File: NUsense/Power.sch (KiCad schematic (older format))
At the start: 13 parts

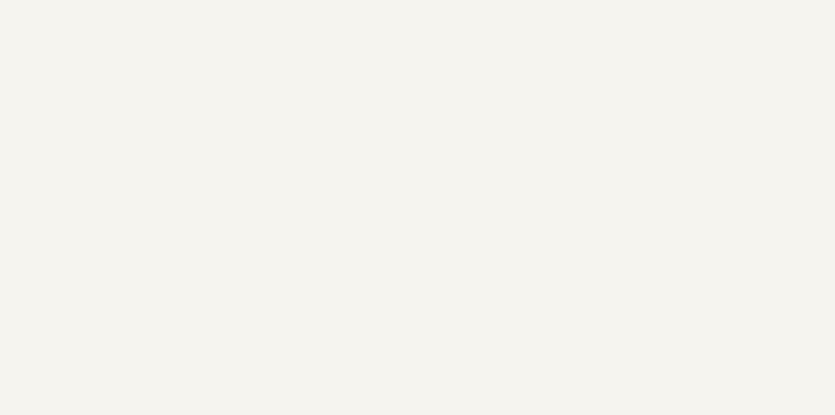
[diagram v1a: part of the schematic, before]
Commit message: Add power components
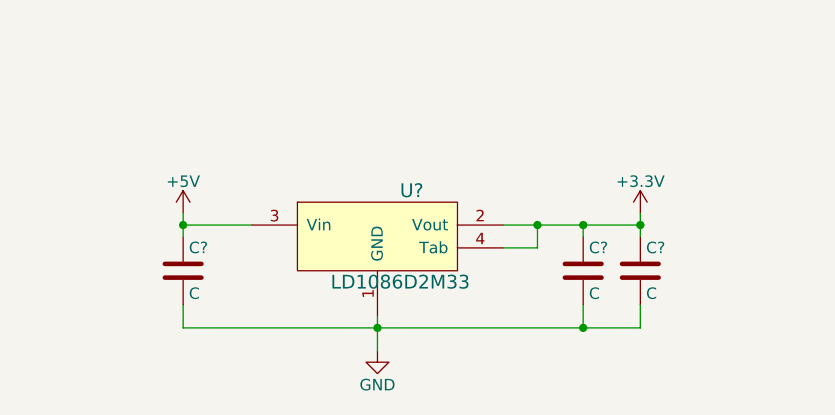
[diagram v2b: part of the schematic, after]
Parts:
- added C? (x3): C, symbol C
- added U?: LD1086D2M33, symbol LD1086D2M33
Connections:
- net labels added: +3.3V, +5V
- wire segments 40 -> 52
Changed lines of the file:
@@
 Text GLabel 5400 2150 1    60   Input ~ 0
 I-
+$Comp
+L +5V #PWR?
+U 1 1 5A71CFBC
+P 1900 6250
+F 0 "#PWR?" H 1900 6100 50  0001 C CNN
+F 1 "+5V" H 1900 6390 50  0000 C CNN
+F 2 "" H 1900 6250 50  0001 C CNN
+F 3 "" H 1900 6250 50  0001 C CNN
+	1    1900 6250
+	1    0    0    -1
+$EndComp
+$Comp
+L +3.3V #PWR?
+U 1 1 5A71CFF7
+P 3900 6250
+F 0 "#PWR?" H 3900 6100 50  0001 C CNN
+F 1 "+3.3V" H 3900 6390 50  0000 C CNN
+F 2 "" H 3900 6250 50  0001 C CNN
+F 3 "" H 3900 6250 50  0001 C CNN
+	1    3900 6250
+	1    0    0    -1
+$EndComp
+$Comp
+L GND #PWR?
+U 1 1 5A71D094
+P 2750 6850
+F 0 "#PWR?" H 2750 6600 50  0001 C CNN
+F 1 "GND" H 2750 6700 50  0000 C CNN
+F 2 "" H 2750 6850 50  0001 C CNN
+F 3 "" H 2750 6850 50  0001 C CNN
+	1    2750 6850
+	1    0    0    -1
+$EndComp
+$Comp
+L C C?
+U 1 1 5A71D0C2
+P 1900 6500
+F 0 "C?" H 1925 6600 50  0000 L CNN
+F 1 "C" H 1925 6400 50  0000 L CNN
+F 2 "" H 1938 6350 50  0001 C CNN
+F 3 "" H 1900 6500 50  0001 C CNN
+	1    1900 6500
+	1    0    0    -1
+$EndComp
+$Comp
+L C C?
+U 1 1 5A71D111
+P 3900 6500
+F 0 "C?" H 3925 6600 50  0000 L CNN
+F 1 "C" H 3925 6400 50  0000 L CNN
+F 2 "" H 3938 6350 50  0001 C CNN
+F 3 "" H 3900 6500 50  0001 C CNN
+	1    3900 6500
+	1    0    0    -1
+$EndComp
+$Comp
+L C C?
+U 1 1 5A71D62F
+P 3650 6500
+F 0 "C?" H 3675 6600 50  0000 L CNN
+F 1 "C" H 3675 6400 50  0000 L CNN
+F 2 "" H 3688 6350 50  0001 C CNN
+F 3 "" H 3650 6500 50  0001 C CNN
+	1    3650 6500
+	1    0    0    -1
+$EndComp
+Wire Wire Line
+	3650 6350 3650 6300
+Wire Wire Line
+	3300 6300 3900 6300
+Wire Wire Line
+	3900 6250 3900 6350
+Connection ~ 3900 6300
+Wire Wire Line
+	3900 6750 3900 6650
+Wire Wire Line
+	1900 6750 3900 6750
+Wire Wire Line
+	2750 6700 2750 6850
+Wire Wire Line
+	3650 6650 3650 6750
+Connection ~ 3650 6750
+Wire Wire Line
+	1900 6650 1900 6750
+Connection ~ 2750 6750
+Wire Wire Line
+	1900 6250 1900 6350
+$Comp
+L LD1086D2M33 U?
+U 1 1 5A71F0BD
+P 2400 6500
+F 0 "U?" H 2900 6850 60  0000 C CNN
+F 1 "LD1086D2M33" H 2850 6450 60  0000 C CNN
+F 2 "" H 2400 6500 60  0001 C CNN
+F 3 "" H 2400 6500 60  0001 C CNN
+	1    2400 6500
+	1    0    0    -1
+$EndComp
+Wire Wire Line
+	2200 6300 1900 6300
+Connection ~ 1900 6300
+Wire Wire Line
+	3300 6400 3450 6400
+Wire Wire Line
+	3450 6400 3450 6300
+Connection ~ 3650 6300
+Connection ~ 3450 6300
 $EndSCHEMATC

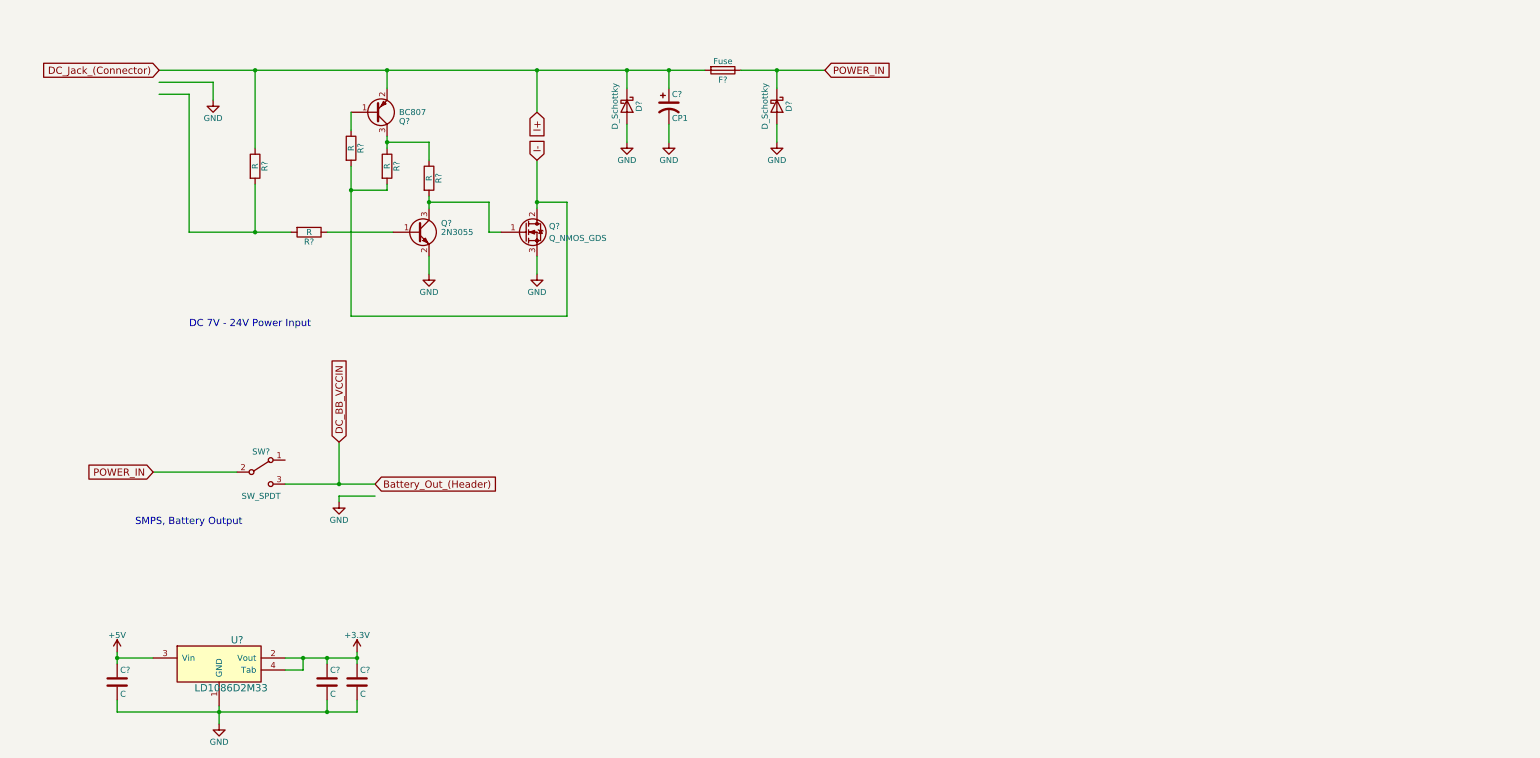
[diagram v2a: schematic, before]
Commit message: Update component values
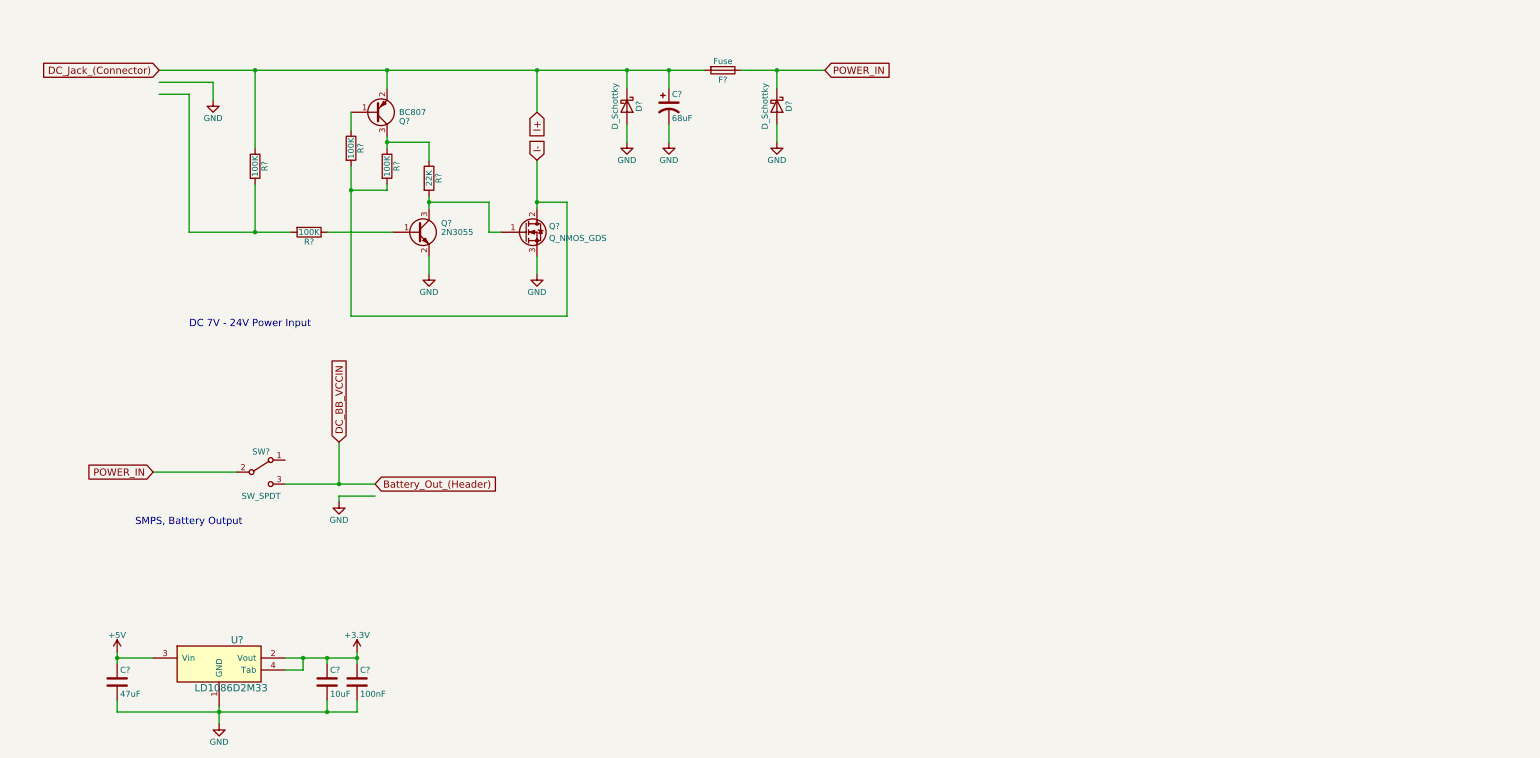
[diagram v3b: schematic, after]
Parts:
- C?: value CP1 -> 68uF
- C?: value C -> 47uF
- C?: value C -> 100nF
- C?: value C -> 10uF
- R? (x4): value R -> 100K
- R?: value R -> 22K
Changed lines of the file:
@@
 P 3050 2200
 F 0 "R?" V 3130 2200 50  0000 C CNN
-F 1 "R" V 3050 2200 50  0000 C CNN
+F 1 "100K" V 3050 2200 50  0000 C CNN
 F 2 "" V 2980 2200 50  0001 C CNN
 F 3 "" H 3050 2200 50  0001 C CNN
@@
 P 3500 2750
 F 0 "R?" V 3580 2750 50  0000 C CNN
-F 1 "R" V 3500 2750 50  0000 C CNN
+F 1 "100K" V 3500 2750 50  0000 C CNN
 F 2 "" V 3430 2750 50  0001 C CNN
 F 3 "" H 3500 2750 50  0001 C CNN
@@
 P 4500 2300
 F 0 "R?" V 4580 2300 50  0000 C CNN
-F 1 "R" V 4500 2300 50  0000 C CNN
+F 1 "22K" V 4500 2300 50  0000 C CNN
 F 2 "" V 4430 2300 50  0001 C CNN
 F 3 "" H 4500 2300 50  0001 C CNN
@@
 P 4150 2200
 F 0 "R?" V 4230 2200 50  0000 C CNN
-F 1 "R" V 4150 2200 50  0000 C CNN
+F 1 "100K" V 4150 2200 50  0000 C CNN
 F 2 "" V 4080 2200 50  0001 C CNN
 F 3 "" H 4150 2200 50  0001 C CNN
@@
 P 3850 2050
 F 0 "R?" V 3930 2050 50  0000 C CNN
-F 1 "R" V 3850 2050 50  0000 C CNN
+F 1 "100K" V 3850 2050 50  0000 C CNN
 F 2 "" V 3780 2050 50  0001 C CNN
 F 3 "" H 3850 2050 50  0001 C CNN
@@
 P 6500 1700
 F 0 "C?" H 6525 1800 50  0000 L CNN
-F 1 "CP1" H 6525 1600 50  0000 L CNN
+F 1 "68uF" H 6525 1600 50  0000 L CNN
 F 2 "" H 6500 1700 50  0001 C CNN
 F 3 "" H 6500 1700 50  0001 C CNN
@@
 P 1900 6500
 F 0 "C?" H 1925 6600 50  0000 L CNN
-F 1 "C" H 1925 6400 50  0000 L CNN
+F 1 "47uF" H 1925 6400 50  0000 L CNN
 F 2 "" H 1938 6350 50  0001 C CNN
 F 3 "" H 1900 6500 50  0001 C CNN
@@
 P 3900 6500
 F 0 "C?" H 3925 6600 50  0000 L CNN
-F 1 "C" H 3925 6400 50  0000 L CNN
+F 1 "100nF" H 3925 6400 50  0000 L CNN
 F 2 "" H 3938 6350 50  0001 C CNN
 F 3 "" H 3900 6500 50  0001 C CNN
@@
 P 3650 6500
 F 0 "C?" H 3675 6600 50  0000 L CNN
-F 1 "C" H 3675 6400 50  0000 L CNN
+F 1 "10uF" H 3675 6400 50  0000 L CNN
 F 2 "" H 3688 6350 50  0001 C CNN
 F 3 "" H 3650 6500 50  0001 C CNN

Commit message: Correct Broken Files
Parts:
- added C?: 0.1uF, symbol C
- added C?: 1uF, symbol C
- added D? (x2): D_Schottky, symbol D_Schottky
- added Q?: Q_PMOS_GDS, symbol Q_PMOS_GDS
- added Q?: 2N2219, TO_SOT_Packages_THT:TO-39-3, symbol 2N2219
- added R? (x2): 47K, symbol R
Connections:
- net labels added: DXL_PWR, DXL_PWR_EN
- wire segments 52 -> 70
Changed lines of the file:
@@
 Connection ~ 3650 6300
 Connection ~ 3450 6300
+Text GLabel 9800 4500 0    60   Input ~ 0
+DXL_PWR_EN
+$Comp
+L R R?
+U 1 1 5A7104F8
+P 10600 3850
+F 0 "R?" V 10680 3850 50  0000 C CNN
+F 1 "47K" V 10600 3850 50  0000 C CNN
+F 2 "" V 10530 3850 50  0001 C CNN
+F 3 "" H 10600 3850 50  0001 C CNN
+	1    10600 3850
+	1    0    0    -1
+$EndComp
+$Comp
+L C C?
+U 1 1 5A7104FF
+P 11250 4500
+F 0 "C?" H 11275 4600 50  0000 L CNN
+F 1 "0.1uF" H 11275 4400 50  0000 L CNN
+F 2 "" H 11288 4350 50  0001 C CNN
+F 3 "" H 11250 4500 50  0001 C CNN
+	1    11250 4500
+	1    0    0    -1
+$EndComp
+$Comp
+L R R?
+U 1 1 5A710506
+P 13550 4200
+F 0 "R?" V 13630 4200 50  0000 C CNN
+F 1 "47K" V 13550 4200 50  0000 C CNN
+F 2 "" V 13480 4200 50  0001 C CNN
+F 3 "" H 13550 4200 50  0001 C CNN
+	1    13550 4200
+	1    0    0    -1
+$EndComp
+Text GLabel 11850 3200 0    60   Input ~ 0
+DC_BB_VCCIN
+$Comp
+L D_Schottky D?
+U 1 1 5A71050E
+P 12450 4200
+F 0 "D?" H 12450 4300 50  0000 C CNN
+F 1 "D_Schottky" H 12450 4100 50  0000 C CNN
+F 2 "" H 12450 4200 50  0001 C CNN
+F 3 "" H 12450 4200 50  0001 C CNN
+	1    12450 4200
+	0    1    1    0
+$EndComp
+$Comp
+L D_Schottky D?
+U 1 1 5A710515
+P 13000 4200
+F 0 "D?" H 13000 4300 50  0000 C CNN
+F 1 "D_Schottky" H 13000 4100 50  0000 C CNN
+F 2 "" H 13000 4200 50  0001 C CNN
+F 3 "" H 13000 4200 50  0001 C CNN
+	1    13000 4200
+	0    1    1    0
+$EndComp
+$Comp
+L C C?
+U 1 1 5A71051C
+P 13000 3750
+F 0 "C?" H 13025 3850 50  0000 L CNN
+F 1 "1uF" H 13025 3650 50  0000 L CNN
+F 2 "" H 13038 3600 50  0001 C CNN
+F 3 "" H 13000 3750 50  0001 C CNN
+	1    13000 3750
+	1    0    0    -1
+$EndComp
+$Comp
+L Q_PMOS_GDS Q?
+U 1 1 5A710523
+P 11750 4150
+F 0 "Q?" H 11950 4200 50  0000 L CNN
+F 1 "Q_PMOS_GDS" H 11950 4100 50  0000 L CNN
+F 2 "" H 11950 4250 50  0001 C CNN
+F 3 "" H 11750 4150 50  0001 C CNN
+	1    11750 4150
+	1    0    0    1
+$EndComp
+$Comp
+L 2N2219 Q?
+U 1 1 5A71052A
+P 10500 4500
+F 0 "Q?" H 10700 4575 50  0000 L CNN
+F 1 "2N2219" H 10700 4500 50  0000 L CNN
+F 2 "TO_SOT_Packages_THT:TO-39-3" H 10700 4425 50  0001 L CIN
+F 3 "" H 10500 4500 50  0001 L CNN
+	1    10500 4500
+	1    0    0    -1
+$EndComp
+Wire Wire Line
+	11850 4350 11850 5100
+Wire Wire Line
+	11250 4900 13550 4900
+Wire Wire Line
+	11250 4900 11250 4650
+Wire Wire Line
+	13550 4900 13550 4350
+Connection ~ 11850 4900
+Wire Wire Line
+	10600 3700 10600 3400
+Wire Wire Line
+	10600 3400 13550 3400
+Wire Wire Line
+	13550 3400 13550 4050
+Wire Wire Line
+	11850 3200 11850 3950
+Connection ~ 11850 3400
+Wire Wire Line
+	11550 4150 10600 4150
+Wire Wire Line
+	11250 4350 11250 4150
+Connection ~ 11250 4150
+Wire Wire Line
+	12450 4050 12450 3400
+Connection ~ 12450 3400
+Wire Wire Line
+	13000 3600 13000 3400
+Connection ~ 13000 3400
+Wire Wire Line
+	13000 3900 13000 4050
+Wire Wire Line
+	13000 4350 13000 4900
+Connection ~ 13000 4900
+Wire Wire Line
+	12450 4350 12450 4900
+Connection ~ 12450 4900
+Wire Wire Line
+	10600 4000 10600 4300
+Connection ~ 10600 4150
+$Comp
+L GND #PWR?
+U 1 1 5A710549
+P 10600 4950
+F 0 "#PWR?" H 10600 4700 50  0001 C CNN
+F 1 "GND" H 10600 4800 50  0000 C CNN
+F 2 "" H 10600 4950 50  0001 C CNN
+F 3 "" H 10600 4950 50  0001 C CNN
+	1    10600 4950
+	1    0    0    -1
+$EndComp
+Wire Wire Line
+	10600 4950 10600 4700
+Wire Wire Line
+	10300 4500 9800 4500
+Text HLabel 11850 5100 0    60   Output ~ 0
+DXL_PWR
 $EndSCHEMATC

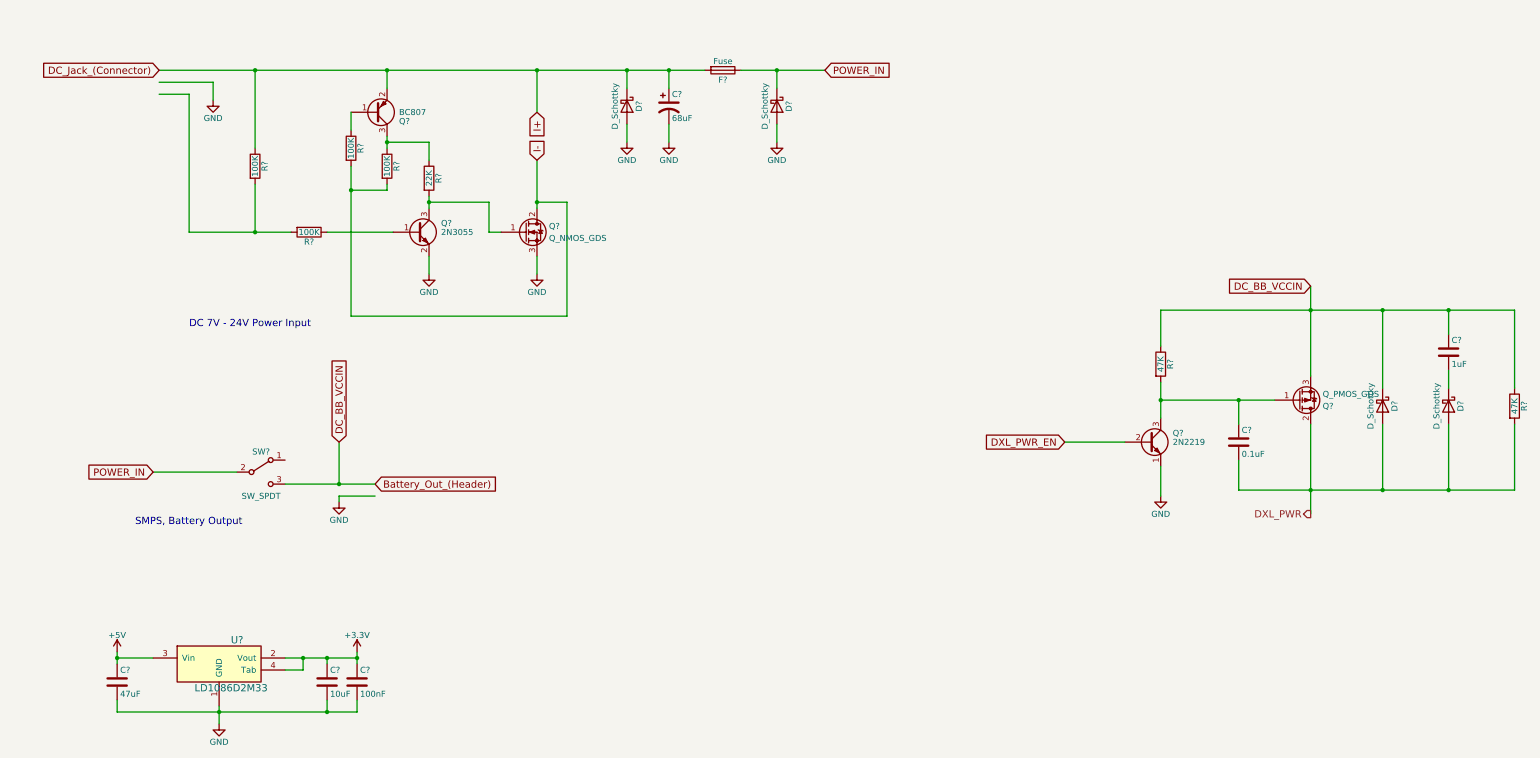
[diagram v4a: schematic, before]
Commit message: Adds annotations and footprints to all components
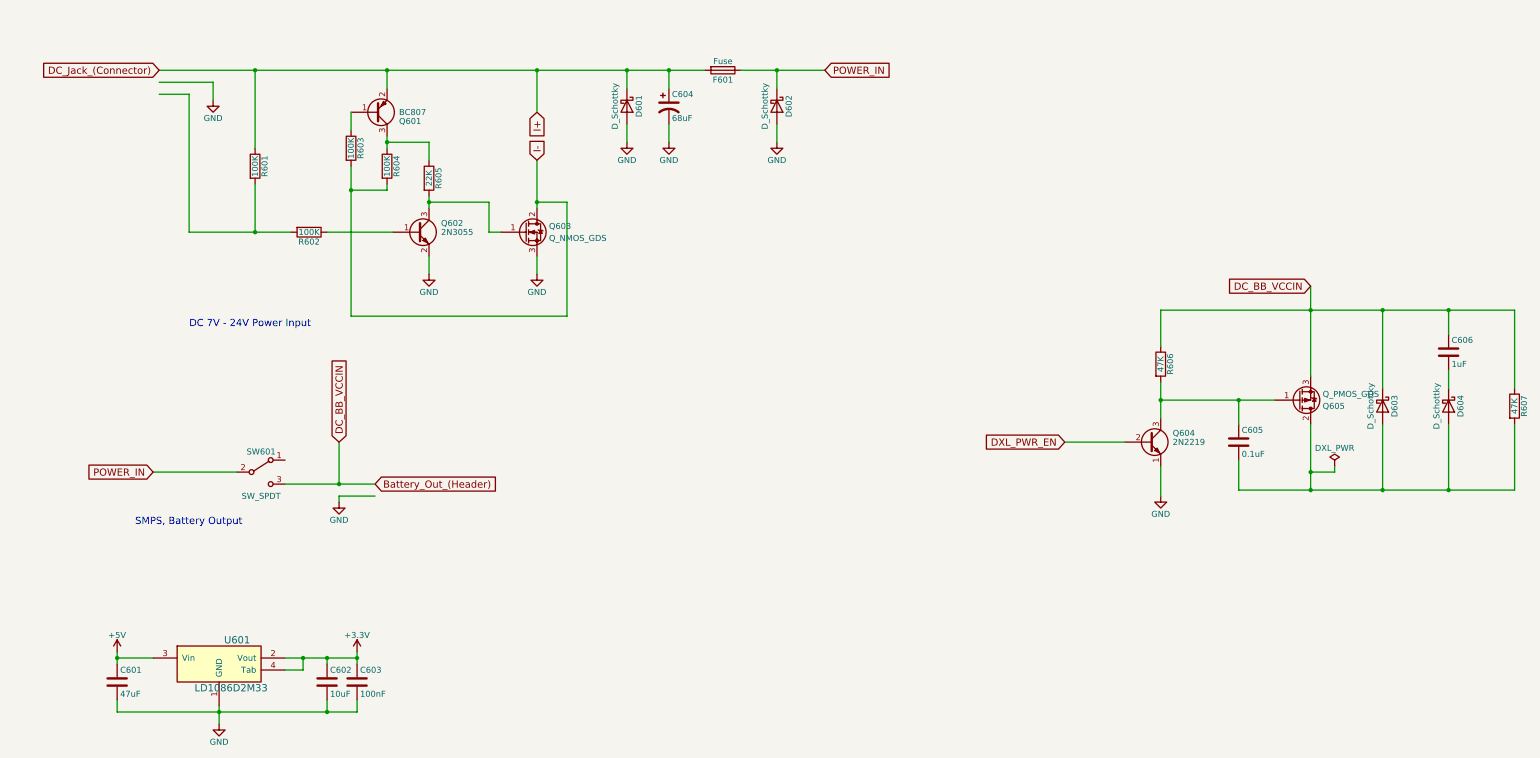
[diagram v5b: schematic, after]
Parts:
- C601, C602, C603, C604, C605, C606: renamed from C?; footprint (none) -> Capacitors_SMD:C_0805_HandSoldering
- Q602: renamed from Q?; footprint TO_SOT_Packages_THT:TO-3 -> TO_SOT_Packages_SMD:SOT-23
- Q603, Q605: renamed from Q?; footprint (none) -> Footprints:D2PAK
- Q604: renamed from Q?; footprint TO_SOT_Packages_THT:TO-39-3 -> TO_SOT_Packages_SMD:SOT-23
- R601, R602, R603, R604, R605, R606, R607: renamed from R?; footprint (none) -> Resistors_SMD:R_0805_HandSoldering
- U601: renamed from U?; footprint (none) -> Footprints:D2PAK
- gave numbers to parts that had none: 7
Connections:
- net labels removed: DXL_PWR
- wire segments 70 -> 72

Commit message: More Changes
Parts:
- removed F601: Fuse, symbol Fuse
- added C1205: 47nF, Capacitors_SMD:C_0805_HandSoldering, symbol C
- added C1206, C1207, C1208, C1209: 330uF, symbol CP1
- added F1201: Fuse, symbol Fuse
- added H1201: DC_JACK, symbol DC_JACK
- added H1202: NUC_PWR, symbol NUC_PWR
- added H1203: BATT_PLUG, symbol BATT_PLUG
- added Q1204: Q_NMOS_GDS, symbol Q_NMOS_GDS
- added R1206: 10, symbol R
- added R1207: 100K, symbol R
- renumbered C601 to C1201, C602 to C1202, C603 to C1203, C604 to C1204, C605 to C1210, C606 to C1211, D601 to D1201, D602 to D1202, D603 to D1203, D604 to D1204, Q601 to Q1201, Q602 to Q1202, Q603 to Q1203, Q604 to Q1205, Q605 to Q1206, R601 to R1201, R602 to R1202, R603 to R1203, R604 to R1204, R605 to R1205, R606 to R1208, R607 to R1209, SW601 to SW1201, U601 to U1201
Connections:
- net labels added: BATT_+, BATT_-
- net labels removed: Battery_Out_(Header), DC_BB_VCCIN, DC_Jack_(Connector), I+, I-, POWER_IN
- wire segments 72 -> 91
